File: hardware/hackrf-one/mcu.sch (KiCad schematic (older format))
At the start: 113 parts, among them J1 GSG-USB-MICRO-B, P1 1V8, P13 VBUS, P17 SSP0, P20 GPIO, P21 ANALOG, P22 I2S, P23 DBGEN, P24 TRST, P25 LPC_ISP, P26 LPC_JTAG, P28 SD, P29 CPLD_JTAG, P3 GND, P30 BANK2_AUX, P31 BANK1_AUX, P5 WAKEUP, P7 RTC, P8 VCC, SW1 DFU, SW2 RESET, U20 W25Q80BV, U21 TPS62410, U22 GSG-IP4220CZ6, U23 LPC4320FBD144, U24 GSG-XC2C64A-7VQG100C, X2 MCU_XTAL, X3 RTC_XTAL

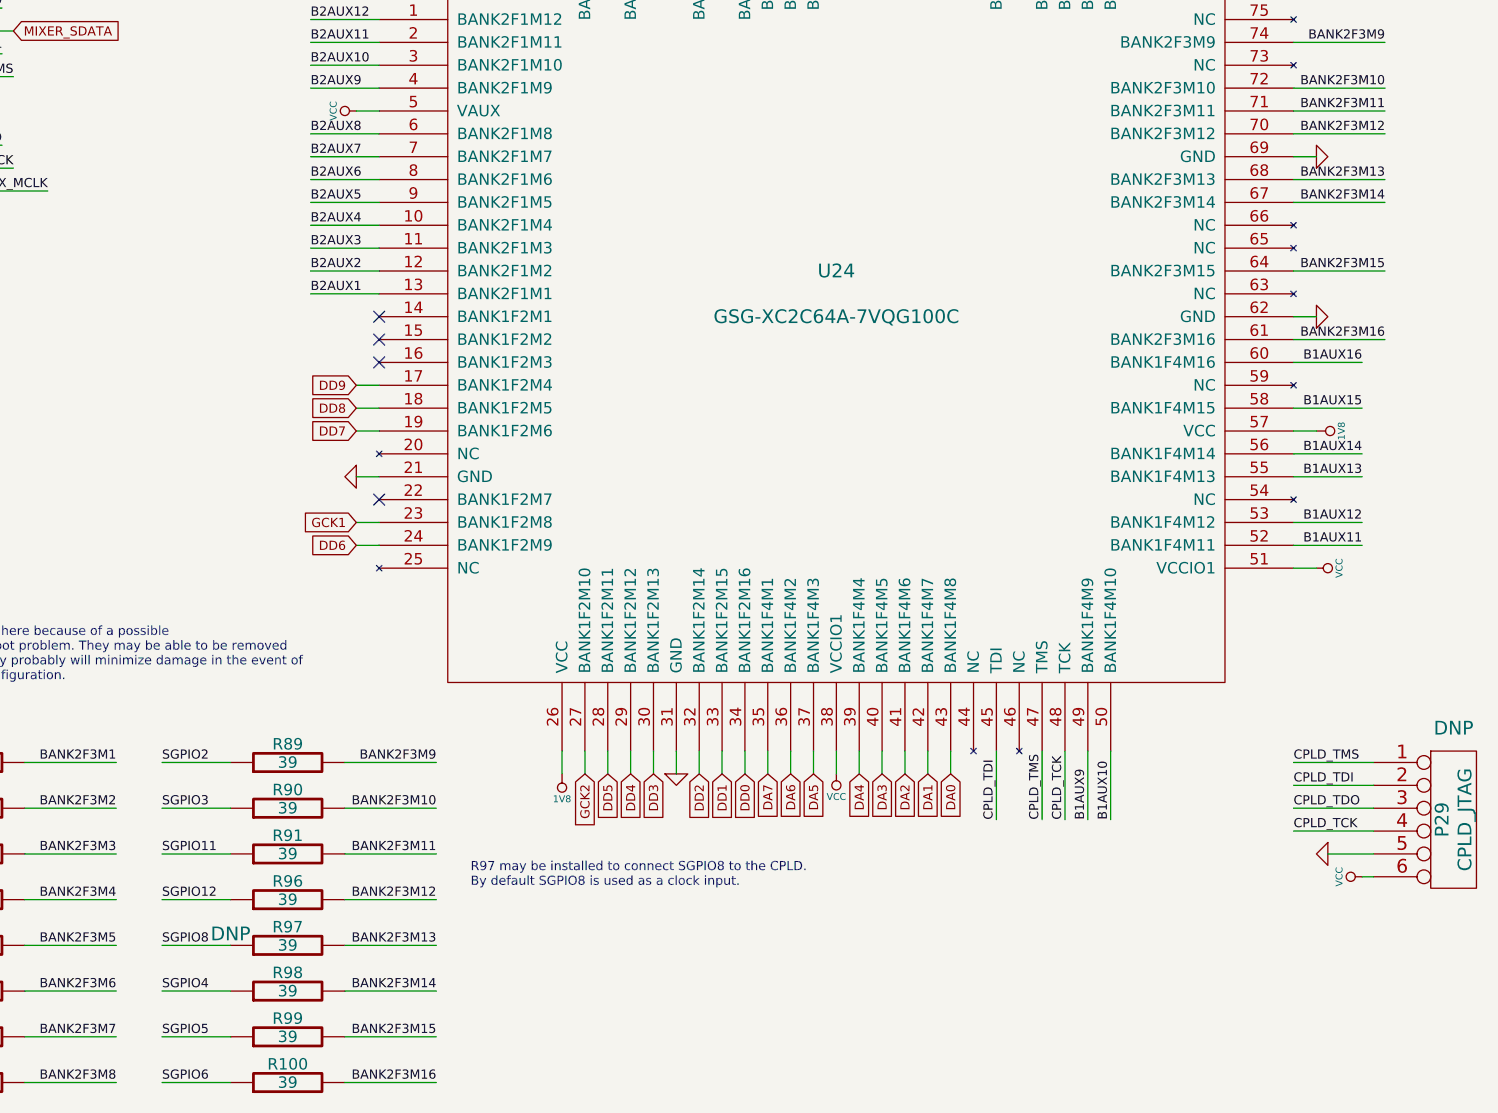
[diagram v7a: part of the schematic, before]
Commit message: LPC4320 placed
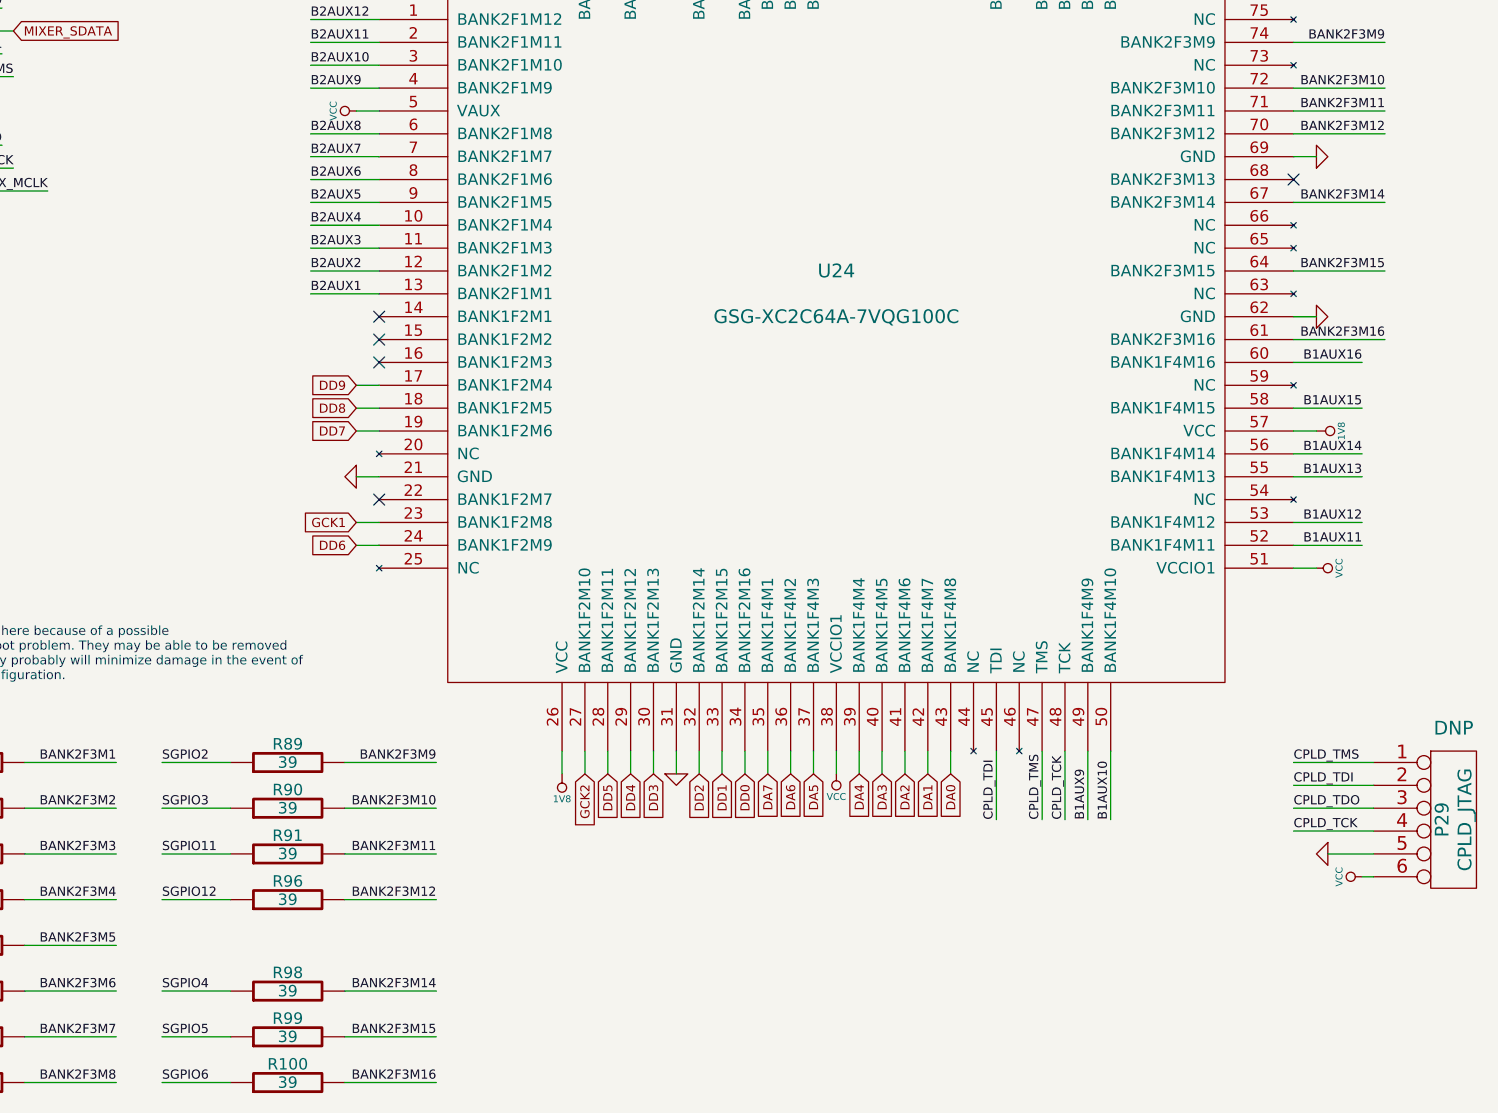
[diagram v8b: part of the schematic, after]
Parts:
- removed R97: 39, symbol R
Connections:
- net BANK2F3M13: no longer names the net of U24.68 (BANK2F3M13)
- no-connect marks 15 -> 16
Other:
- note removed: "R97 may be installed to connect SGPIO8 to the CPLD.\nBy default SGPIO8 is used as a clock input."
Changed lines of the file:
@@
 Text Notes 2200 9200 0    40   ~ 0
 Default boot configuration is SPIFI.\nPress SW1 during reset to switch to\nUSB0 (DFU mode).
-Text Notes 12000 9550 0    40   ~ 0
-R97 may be installed to connect SGPIO8 to the CPLD.\nBy default SGPIO8 is used as a clock input.
 Text GLabel 8750 7750 3    40   Input ~ 0
 SGPIO_CLK
@@
 Text Label 11850 10000 2    40   ~ 0
 BANK2F3M14
-Text Label 16000 6450 2    40   ~ 0
-BANK2F3M13
-Text Label 11850 9800 2    40   ~ 0
-BANK2F3M13
 Text Label 16000 6250 2    40   ~ 0
 BANK2F3M12
@@
 $EndComp
 $Comp
-L R R97
-U 1 1 503F98AA
-P 11200 9800
-F 0 "R97" V 11280 9800 50  0000 C CNN
-F 1 "39" V 11200 9800 50  0000 C CNN
-F 2 "" H 11200 9800 60  0001 C CNN
-F 3 "" H 11200 9800 60  0001 C CNN
-F 4 "Stackpole" H 11200 9800 60  0001 C CNN "Manufacturer"
-F 5 "RMCF0402JT39R0" H 11200 9800 60  0001 C CNN "Part Number"
-F 6 "RES 39 OHM 1/16W 5% 0402 SMD" H 11200 9800 60  0001 C CNN "Description"
-F 7 "DNP" V 11250 10050 60  0000 C CNN "Note"
-	1    11200 9800
-	0    -1   -1   0
-$EndComp
-$Comp
 L R R96
 U 1 1 503F989E
@@
 Text Label 10650 9600 0    40   ~ 0
 SGPIO12
-Text Label 10650 9800 0    40   ~ 0
-SGPIO8
 Text Label 10650 10000 0    40   ~ 0
 SGPIO4
@@
 	10650 9400 10950 9400
 Wire Wire Line
-	10650 9800 10950 9800
-Wire Wire Line
 	10650 10200 10950 10200
 Wire Wire Line
 	11450 10400 11850 10400
 Wire Wire Line
-	11450 9800 11850 9800
-Wire Wire Line
 	11450 10200 11850 10200
 Wire Wire Line
@@
 	15600 6850 16000 6850
 Wire Wire Line
-	15600 6450 16000 6450
-Wire Wire Line
 	15600 6250 16000 6250
 Wire Wire Line
@@
 Connection ~ 1600 3350
 NoConn ~ 11600 7850
+NoConn ~ 15600 6450
 $EndSCHEMATC
